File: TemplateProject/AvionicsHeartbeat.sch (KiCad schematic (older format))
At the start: 30 parts, among them Q1 Q_NMOS_GDS, Q2 Q_PMOS_GDS, U1 74HC21, U2 74HC266, U3 74HC08, U4 74HC21, U5 74LVC1G17, U6 LTC6993xS6-1

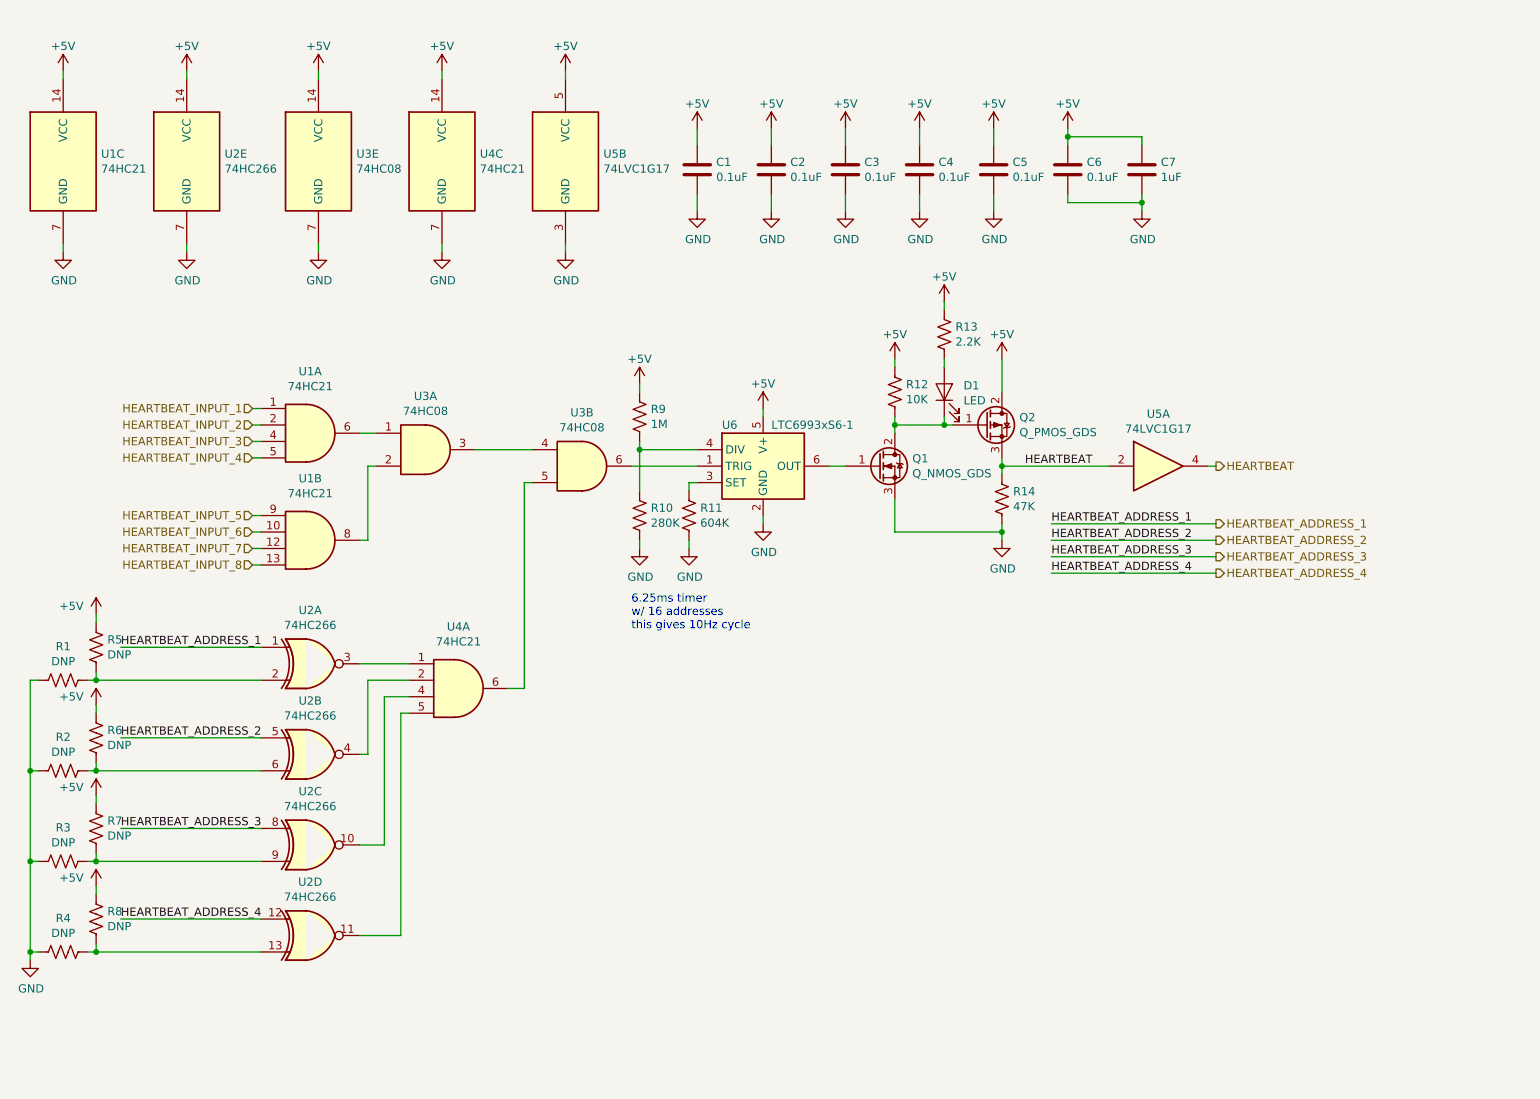
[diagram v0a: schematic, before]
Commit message: Added HEARTBEAT_RESTART signal and resistor
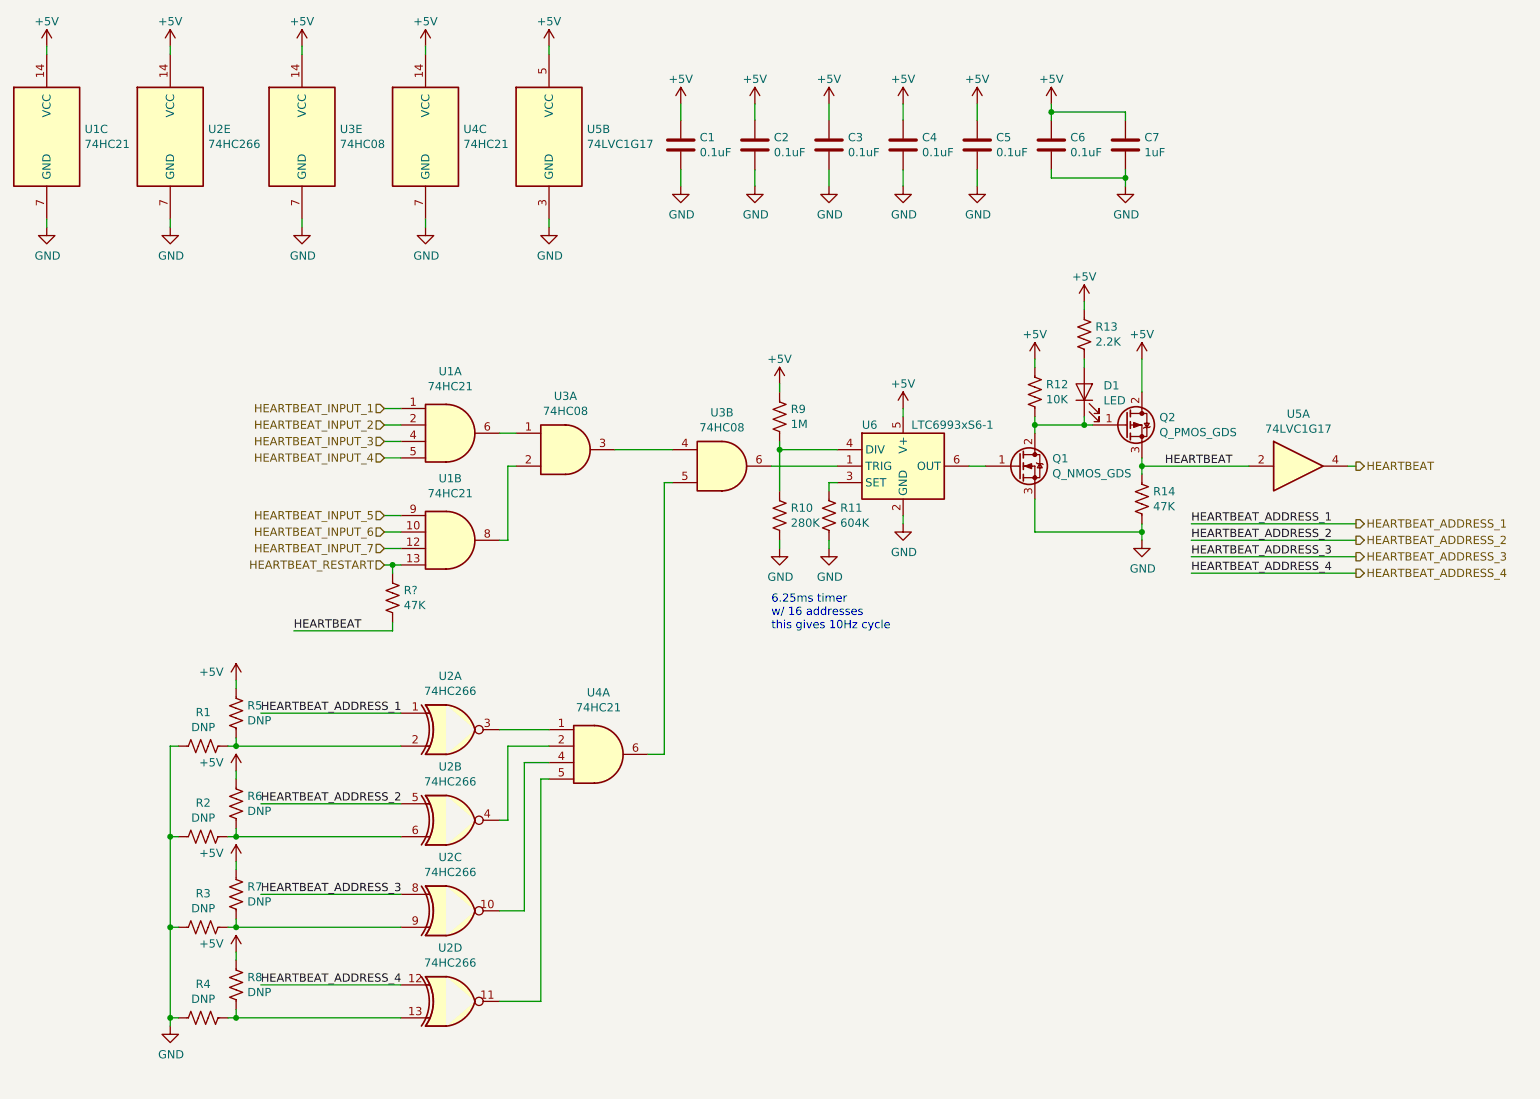
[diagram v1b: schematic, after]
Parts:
- added R?: 47K, symbol Device:R_US
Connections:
- net HEARTBEAT: now also R?.2
- net HEARTBEAT_INPUT_8 renamed HEARTBEAT_RESTART
- net HEARTBEAT_RESTART: now also R?.1
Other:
- moved on the sheet: C1, C2, C3, C4, C5, C6, C7, D1, Q1, Q2, R1, R10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

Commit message: Rearrange QuantumBeat
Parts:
- added D2: GREEN, symbol Device:LED
- added D3: BLUE, symbol Device:LED
- added R16, R17: 1.5K, symbol Device:R_US
- C1, C2, C3, C4, C5, C6: footprint (none) -> Capacitor_SMD:C_0603_1608Metric_Pad1.05x0.95mm_HandSolder; Digikey (none) -> 311-1341-1-ND
- U1, U4: Digikey (none) -> 296-31574-1-ND
- U2: Digikey (none) -> 296-31804-1-ND
- U3: Digikey (none) -> 296-14506-1-ND
- gave numbers to parts that had none: 1
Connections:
- net GND: now also R16.2, R17.2
- net HEARTBEAT: now also D3.2 (A)
- net at U3.3, U3.4: now also D2.2 (A)
- new net: D2.1 (K), R16.1
- new net: D3.1 (K), R17.1
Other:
- note added: "Use stuffing options to select\nboard heartbeat address"
- moved on the sheet: R15, U1A, U1B, U3A

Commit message: Spec all QB parts except resistors and caps
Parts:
- removed D1: LED, symbol Device:LED
- removed R13: 2.2K, symbol Device:R_US
- D2: footprint (none) -> LED_SMD:LED_0805_2012Metric_Pad1.15x1.40mm_HandSolder; Digikey (none) -> 732-4983-1-ND
- D3: footprint (none) -> LED_SMD:LED_0805_2012Metric_Pad1.15x1.40mm_HandSolder; Digikey (none) -> 732-4982-1-ND
- Q1: value Q_NMOS_GDS -> DMG2302UK-7; footprint (none) -> Package_TO_SOT_SMD:SOT-23_Handsoldering; Digikey (none) -> DMG2302UK-7DICT-ND
- Q2: value Q_PMOS_GDS -> DMP2123L-7; footprint (none) -> Package_TO_SOT_SMD:SOT-23_Handsoldering; Digikey (none) -> DMP2123LDICT-ND
- R12: value 10K -> 47K
- R16, R17: value 1.5K -> 1K
- U5: Digikey (none) -> 296-11933-1-ND
- U6: Digikey (none) -> LTC6993CS6-1#TRMPBFCT-ND
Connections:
- net +5V: now also Q2.3 (S); no longer Q2.2 (D)
- net HEARTBEAT: now also Q2.2 (D); no longer Q2.3 (S)
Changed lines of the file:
@@
 F 2 "Package_TO_SOT_SMD:TSOT-23-6" H 6100 2950 50  0001 C CNN
 F 3 "https://www.analog.com/media/en/technical-documentation/data-sheets/69931234fc.pdf" H 6150 3450 50  0001 C CNN
+F 4 "LTC6993CS6-1#TRMPBFCT-ND" H 6100 3350 50  0001 C CNN "Digikey"
 	1    6100 3350
 	1    0    0    -1
@@
 $EndComp
 $Comp
-L Device:Q_PMOS_GDS Q2
-U 1 1 5F9F8BCA
-P 7450 3100
-F 0 "Q2" H 7656 3146 50  0000 L CNN
-F 1 "Q_PMOS_GDS" H 7656 3055 50  0000 L CNN
-F 2 "" H 7650 3200 50  0001 C CNN
-F 3 "~" H 7450 3100 50  0001 C CNN
-	1    7450 3100
-	1    0    0    -1
-$EndComp
-$Comp
 L Device:R_US R12
 U 1 1 5F9FA332
 P 6900 2900
 F 0 "R12" H 6968 2946 50  0000 L CNN
-F 1 "10K" H 6968 2855 50  0000 L CNN
+F 1 "47K" H 6968 2855 50  0000 L CNN
 F 2 "" V 6940 2890 50  0001 C CNN
 F 3 "~" H 6900 2900 50  0001 C CNN
@@
 Wire Wire Line
 	6900 3050 6900 3100
-Wire Wire Line
-	6900 3100 7200 3100
 Wire Wire Line
 	6900 2750 6900 2700
@@
 P 6800 3350
 F 0 "Q1" H 7006 3396 50  0000 L CNN
-F 1 "Q_NMOS_GDS" H 7006 3305 50  0000 L CNN
-F 2 "" H 7000 3450 50  0001 C CNN
-F 3 "~" H 6800 3350 50  0001 C CNN
+F 1 "DMG2302UK-7" H 7006 3305 50  0000 L CNN
+F 2 "Package_TO_SOT_SMD:SOT-23_Handsoldering" H 7000 3450 50  0001 C CNN
+F 3 "https://www.diodes.com/assets/Datasheets/DMG2302UK.pdf" H 6800 3350 50  0001 C CNN
+F 4 "DMG2302UK-7DICT-ND" H 6800 3350 50  0001 C CNN "Digikey"
 	1    6800 3350
 	1    0    0    -1
@@
 F 1 "74LVC1G17" H 8500 3576 50  0000 C CNN
 F 2 "Package_TO_SOT_SMD:SOT-23-5_HandSoldering" H 8500 3350 50  0001 C CNN
-F 3 "https://www.ti.com/general/docs/suppproductinfo.tsp?distId=10&gotoUrl=http%3A%2F%2Fwww.ti.com%2Flit%2Fgpn%2Fsn74lvc1g17" H 8500 3350 50  0001 C CNN
+F 3 "https://www.ti.com/lit/ds/symlink/sn74lvc1g17.pdf?HQS=TI-null-null-digikeymode-df-pf-null-wwe&ts=1605119972692" H 8500 3350 50  0001 C CNN
+F 4 "296-11933-1-ND" H 8500 3350 50  0001 C CNN "Digikey"
 	1    8500 3350
 	1    0    0    -1
@@
 Wire Wire Line
 	8800 3350 8850 3350
-Text HLabel 8900 3350 2    50   Output ~ 0
+Text HLabel 9000 3350 2    50   Output ~ 0
 HEARTBEAT
 $Comp
@@
 F 1 "74LVC1G17" H 4180 1305 50  0000 L CNN
 F 2 "Package_TO_SOT_SMD:SOT-23-5_HandSoldering" H 3950 1350 50  0001 C CNN
-F 3 "https://www.ti.com/general/docs/suppproductinfo.tsp?distId=10&gotoUrl=http%3A%2F%2Fwww.ti.com%2Flit%2Fgpn%2Fsn74lvc1g17" H 3950 1350 50  0001 C CNN
+F 3 "https://www.ti.com/lit/ds/symlink/sn74lvc1g17.pdf?HQS=TI-null-null-digikeymode-df-pf-null-wwe&ts=1605119972692" H 3950 1350 50  0001 C CNN
 	2    3950 1350
 	1    0    0    -1
@@
 Wire Wire Line
 	7550 3350 8200 3350
-$Comp
-L Device:LED D1
-U 1 1 5FADE251
-P 7200 2900
-F 0 "D1" V 7239 2783 50  0000 R CNN
-F 1 "LED" V 7148 2783 50  0000 R CNN
-F 2 "" H 7200 2900 50  0001 C CNN
-F 3 "~" H 7200 2900 50  0001 C CNN
-	1    7200 2900
-	0    -1   -1   0
-$EndComp
-Wire Wire Line
-	7200 3050 7200 3100
-Connection ~ 7200 3100
-Wire Wire Line
-	7200 3100 7250 3100
-$Comp
-L Device:R_US R13
-U 1 1 5FAE6631
-P 7200 2550
-F 0 "R13" H 7268 2596 50  0000 L CNN
-F 1 "2.2K" H 7268 2505 50  0000 L CNN
-F 2 "" V 7240 2540 50  0001 C CNN
-F 3 "~" H 7200 2550 50  0001 C CNN
-	1    7200 2550
-	1    0    0    -1
-$EndComp
-Wire Wire Line
-	7200 2700 7200 2750
-Wire Wire Line
-	7200 2400 7200 2350
-$Comp
-L power:+5V #PWR030
-U 1 1 5FAEDB0A
-P 7200 2350
-F 0 "#PWR030" H 7200 2200 50  0001 C CNN
-F 1 "+5V" H 7200 2500 50  0000 C CNN
-F 2 "" H 7200 2350 50  0001 C CNN
-F 3 "" H 7200 2350 50  0001 C CNN
-	1    7200 2350
-	1    0    0    -1
-$EndComp
 Text Label 2250 4350 0    50   ~ 0
 HEARTBEAT
@@
 F 0 "D2" V 4289 3332 50  0000 R CNN
 F 1 "GREEN" V 4198 3332 50  0000 R CNN
-F 2 "" H 4250 3450 50  0001 C CNN
-F 3 "~" H 4250 3450 50  0001 C CNN
+F 2 "LED_SMD:LED_0805_2012Metric_Pad1.15x1.40mm_HandSolder" H 4250 3450 50  0001 C CNN
+F 3 "https://www.we-online.de/katalog/datasheet/150080GS75000.pdf" H 4250 3450 50  0001 C CNN
+F 4 "732-4983-1-ND" V 4250 3450 50  0001 C CNN "Digikey"
 	1    4250 3450
 	0    -1   -1   0
@@
 P 4250 3800
 F 0 "R16" H 4318 3846 50  0000 L CNN
-F 1 "1.5K" H 4318 3755 50  0000 L CNN
+F 1 "1K" H 4318 3755 50  0000 L CNN
 F 2 "" V 4290 3790 50  0001 C CNN
 F 3 "~" H 4250 3800 50  0001 C CNN
@@
 F 0 "D3" V 8889 3383 50  0000 R CNN
 F 1 "BLUE" V 8798 3383 50  0000 R CNN
-F 2 "" H 8850 3500 50  0001 C CNN
-F 3 "~" H 8850 3500 50  0001 C CNN
+F 2 "LED_SMD:LED_0805_2012Metric_Pad1.15x1.40mm_HandSolder" H 8850 3500 50  0001 C CNN
+F 3 "https://www.we-online.de/katalog/datasheet/150080BS75000.pdf" H 8850 3500 50  0001 C CNN
+F 4 "732-4982-1-ND" V 8850 3500 50  0001 C CNN "Digikey"
 	1    8850 3500
 	0    -1   -1   0
@@
 P 8850 3850
 F 0 "R17" H 8918 3896 50  0000 L CNN
-F 1 "1.5K" H 8918 3805 50  0000 L CNN
+F 1 "1K" H 8918 3805 50  0000 L CNN
 F 2 "" V 8890 3840 50  0001 C CNN
 F 3 "~" H 8850 3850 50  0001 C CNN
@@
 Connection ~ 8850 3350
 Wire Wire Line
-	8850 3350 8900 3350
+	8850 3350 9000 3350
 Text Notes 1800 7100 0    50   ~ 0
 Use stuffing options to select\nboard heartbeat address
@@
 	1    0    0    -1
 $EndComp
+$Comp
+L Device:Q_PMOS_GDS Q2
+U 1 1 5F9F8BCA
+P 7450 3100
+F 0 "Q2" H 7656 3146 50  0000 L CNN
+F 1 "DMP2123L-7" H 7656 3055 50  0000 L CNN
+F 2 "Package_TO_SOT_SMD:SOT-23_Handsoldering" H 7650 3200 50  0001 C CNN
+F 3 "https://www.diodes.com/assets/Datasheets/ds31440.pdf" H 7450 3100 50  0001 C CNN
+F 4 "DMP2123LDICT-ND" H 7450 3100 50  0001 C CNN "Digikey"
+	1    7450 3100
+	1    0    0    1
+$EndComp
+Wire Wire Line
+	6900 3100 7250 3100
 $EndSCHEMATC

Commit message: Clarify QuantumBeat signal names
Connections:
- net HEARTBEAT: no longer D3.2 (A), U5.4
- new net HEARTBEAT_BUFF: D3.2 (A), U5.4
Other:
- moved on the sheet: R1, R2, R3, R4, R5, R6, R7, R8
